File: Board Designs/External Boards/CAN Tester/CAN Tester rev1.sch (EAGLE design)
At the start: 27 parts, among them M1 Minifit, M2 Nanofit, M3 Nanofit-1, M4 Minifit-1, U1 ISOLATED CAN TRANSCIEVER, U3 TEENSY_3.2_SIMPLE, U4 CHARACTER_LCD

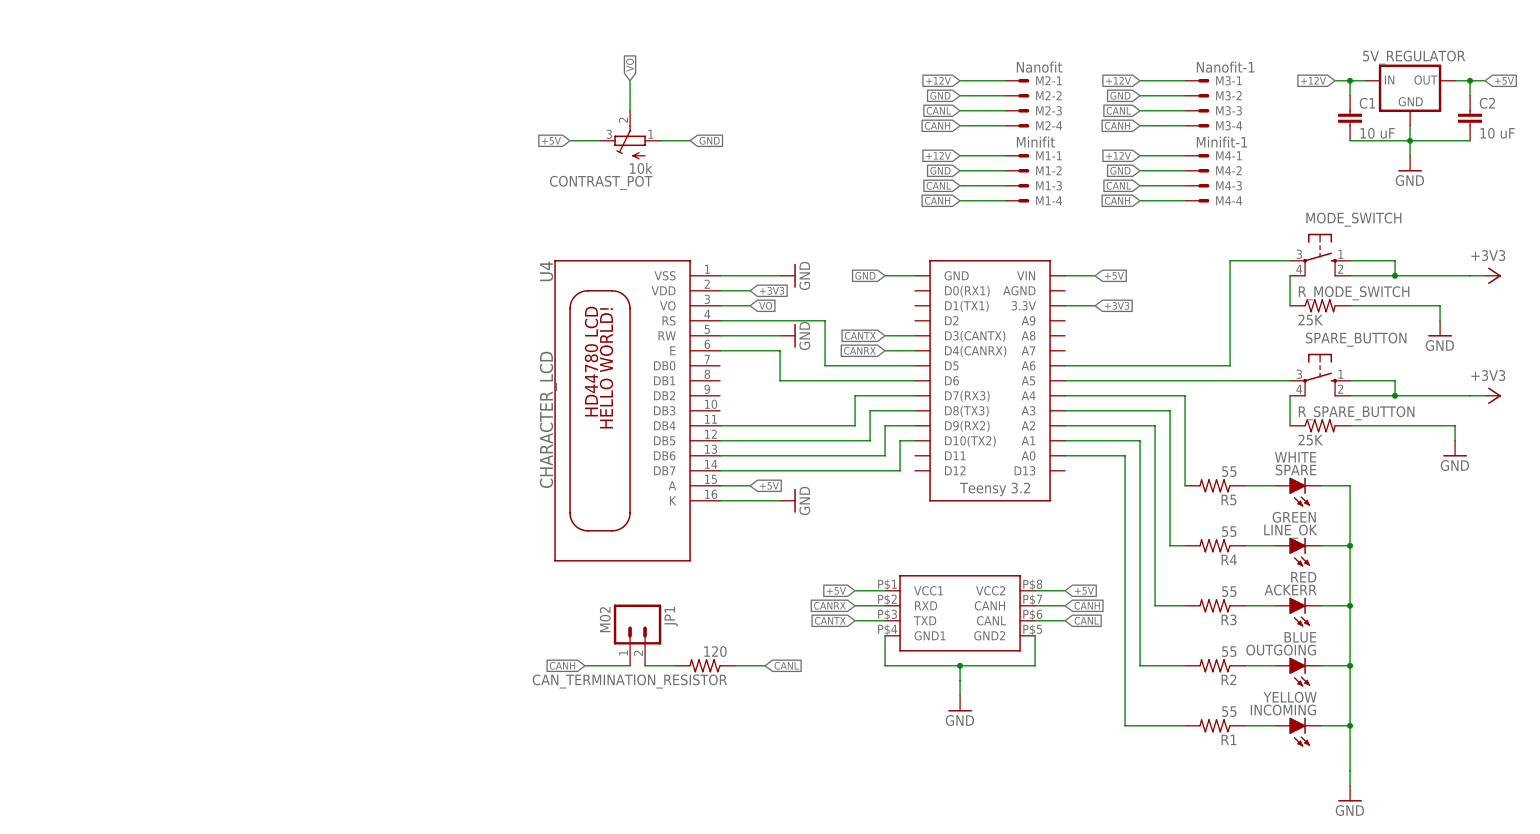
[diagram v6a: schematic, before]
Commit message: Updated CAN Tester board with values for components based on what was available in the shop.
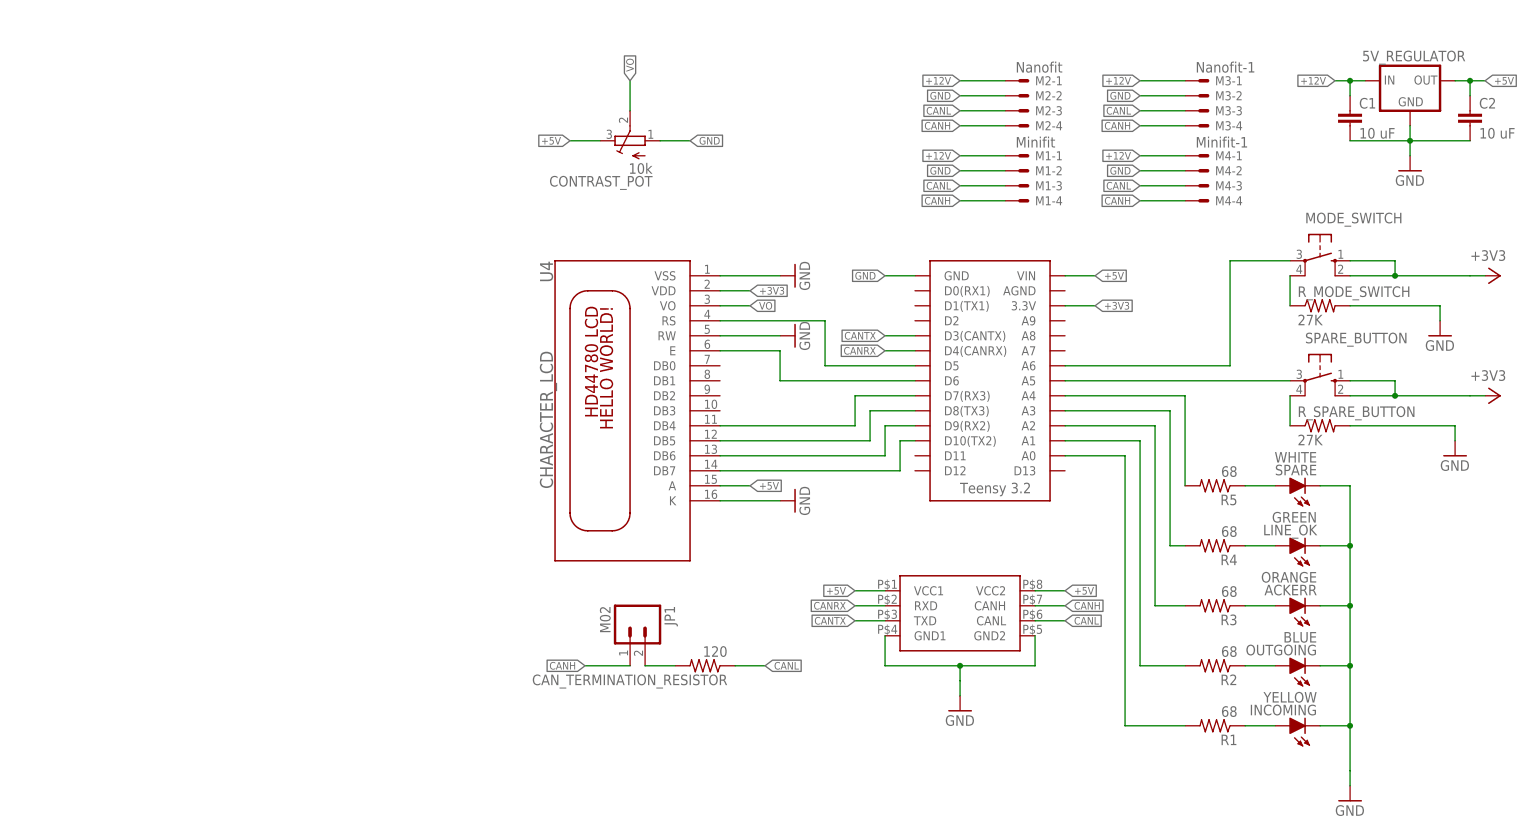
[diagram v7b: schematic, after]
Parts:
- ACKERR: value RED -> ORANGE
- R1, R2, R3, R4, R5: value 55 -> 68
- R_MODE_SWITCH, R_SPARE_BUTTON: value 25K -> 27K

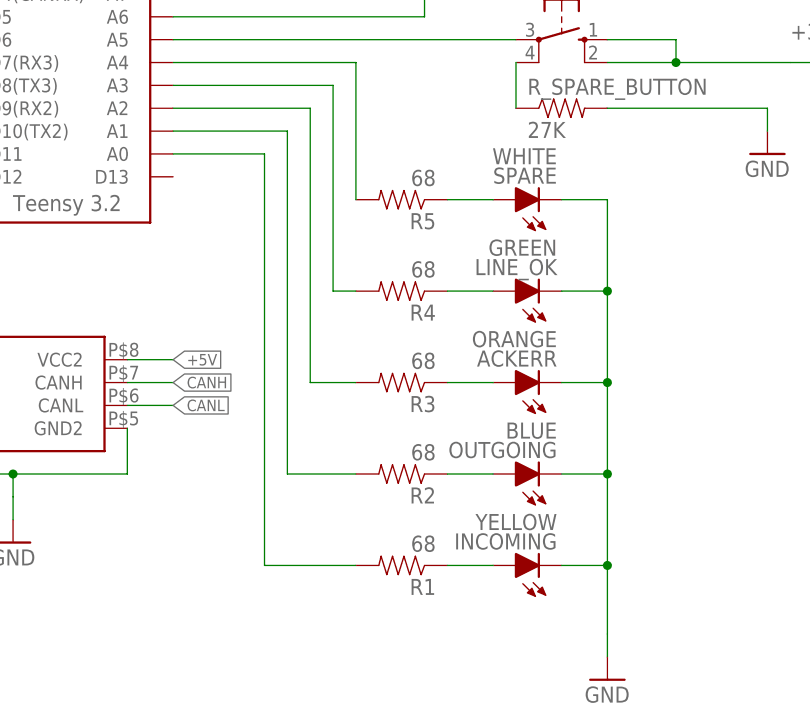
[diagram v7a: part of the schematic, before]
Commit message: Updated resistor values on CAN_Tester to eliminate super bright LED issue
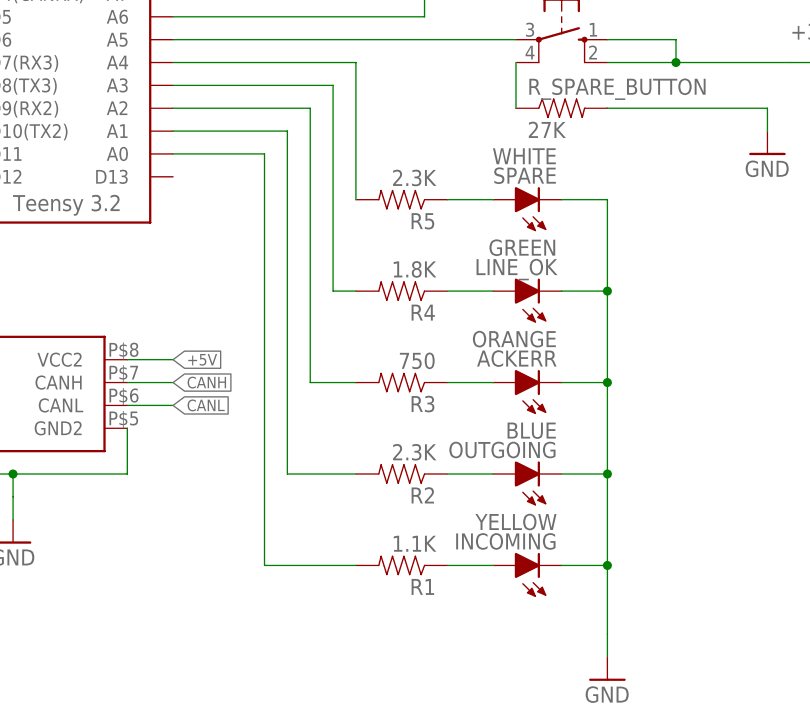
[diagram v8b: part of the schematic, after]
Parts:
- R1: value 68 -> 1.1K
- R2, R5: value 68 -> 2.3K
- R3: value 68 -> 750
- R4: value 68 -> 1.8K
